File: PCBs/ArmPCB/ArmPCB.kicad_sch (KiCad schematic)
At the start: 28 parts, among them J1 Conn_02x07_Odd_Even, J10 Conn_01x04_Pin, J2 Conn_02x08_Odd_Even, J3 Conn_02x08_Odd_Even, J4 Conn_01x04_Pin, J5 Conn_01x02_Pin, J6 Conn_01x03_Pin, J7 Conn_01x03_Pin, J8 Conn_01x03_Pin, J9 Conn_01x04_Pin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

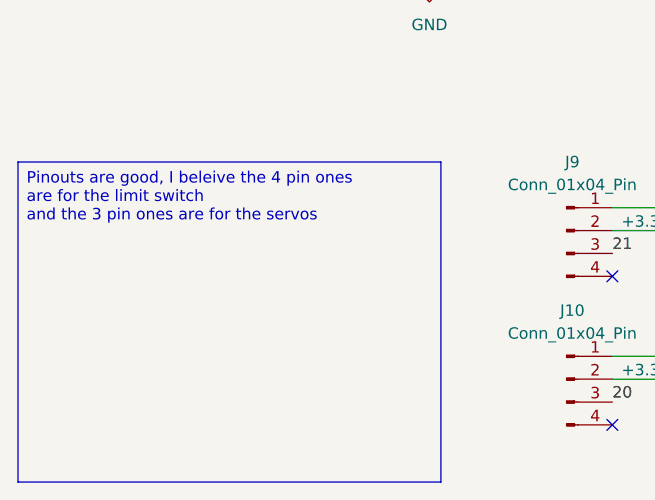
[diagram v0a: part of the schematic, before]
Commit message: Base_Arm_PCB JST FIX
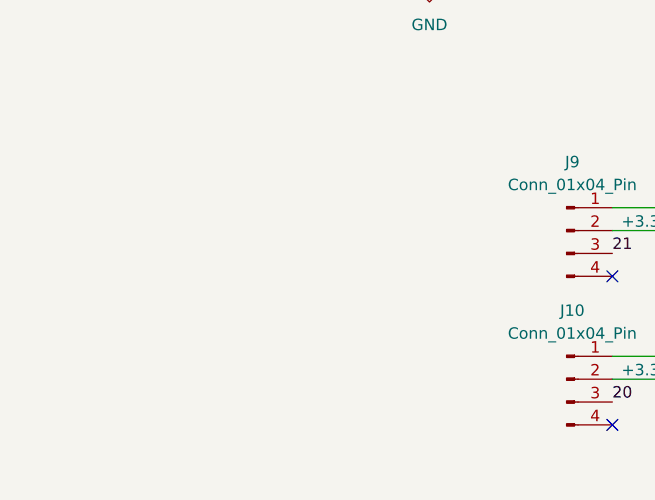
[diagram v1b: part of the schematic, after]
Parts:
- J10, J9: footprint Connector_JST:JST_PH_S4B-PH-K_1x04_P2.00mm_Horizontal -> Connector_JST:JST_GH_SM04B-GHS-TB_1x04-1MP_P1.25mm_Horizontal
- J4: footprint Connector_JST:JST_XH_S4B-XH-A_1x04_P2.50mm_Horizontal -> Connector_JST:JST_GH_SM04B-GHS-TB_1x04-1MP_P1.25mm_Horizontal
- J5: footprint Connector_JST:JST_XH_S2B-XH-A_1x02_P2.50mm_Horizontal -> Connector_JST:JST_GH_SM02B-GHS-TB_1x02-1MP_P1.25mm_Horizontal
- J6, J7, J8: footprint Connector_JST:JST_XH_S3B-XH-A_1x03_P2.50mm_Horizontal -> Connector_JST:JST_GH_SM03B-GHS-TB_1x03-1MP_P1.25mm_Horizontal
